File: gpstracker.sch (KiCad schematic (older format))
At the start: 52 parts, among them IC1 SIM808, J2 Leds, J3 47553-0001, J4 CONN_COAXIAL, J5 CONN_COAXIAL, J6 Micro_SD_Card, Q1 DMP1045U, SW1 Reset, U1 MCP73832-5-OT, U2 ATMEGA328P-AU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

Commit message: More routing
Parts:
- added C19: 100uF, Capacitors_SMD:CP_Elec_6.3x7.7, symbol CP
- C16: footprint Capacitors_Tantalum_SMD:CP_Tantalum_Case-T_EIA-3528-12_Hand -> Capacitors_SMD:CP_Elec_6.3x7.7; Manufacturer (none) -> Panasonic; Manufacturer part number (none) -> EEE-TPC101XAP; Package (none) -> 6.30mm
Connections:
- net +3V3: now also C19.1
- net ARD_HRX: now also U2.10 ((PCINT22/OC0A/AIN0)PD6); no longer U2.9 ((PCINT21/OC0B/T1)PD5)
- net ARD_HTX: now also U2.9 ((PCINT21/OC0B/T1)PD5); no longer U2.10 ((PCINT22/OC0A/AIN0)PD6)
- net GND: now also C19.2
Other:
- moved on the sheet: C15, C2, C5, J6, R14, R15, R4, R5, R6, SW1, U2

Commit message: Redo - Arduino, Sim & power supply
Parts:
- Q1: footprint TO_SOT_Packages_SMD:TO-252-2 -> TO_SOT_Packages_SMD:SOT-23_Handsoldering
- U1: footprint TO_SOT_Packages_SMD:SOT-23-5 -> TO_SOT_Packages_SMD:SOT-23-5_HandSoldering
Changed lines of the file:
@@
 F 0 "U1" H 1300 1550 50  0000 L CNN
 F 1 "MCP73832-5-OT" H 1650 1550 50  0000 L CNN
-F 2 "TO_SOT_Packages_SMD:SOT-23-5" H 1650 1050 50  0001 L CIN
+F 2 "TO_SOT_Packages_SMD:SOT-23-5_HandSoldering" H 1650 1050 50  0001 L CIN
 F 3 "" H 1450 1250 50  0001 C CNN
 	1    1600 1300
@@
 F 0 "Q1" V 4000 1500 50  0000 L CNN
 F 1 "DMP1045U" V 4100 1350 50  0000 L CNN
-F 2 "TO_SOT_Packages_SMD:TO-252-2" H 4000 1550 50  0001 C CNN
+F 2 "TO_SOT_Packages_SMD:SOT-23_Handsoldering" H 4000 1550 50  0001 C CNN
 F 3 "" H 3800 1450 50  0001 C CNN
 	1    3800 1450

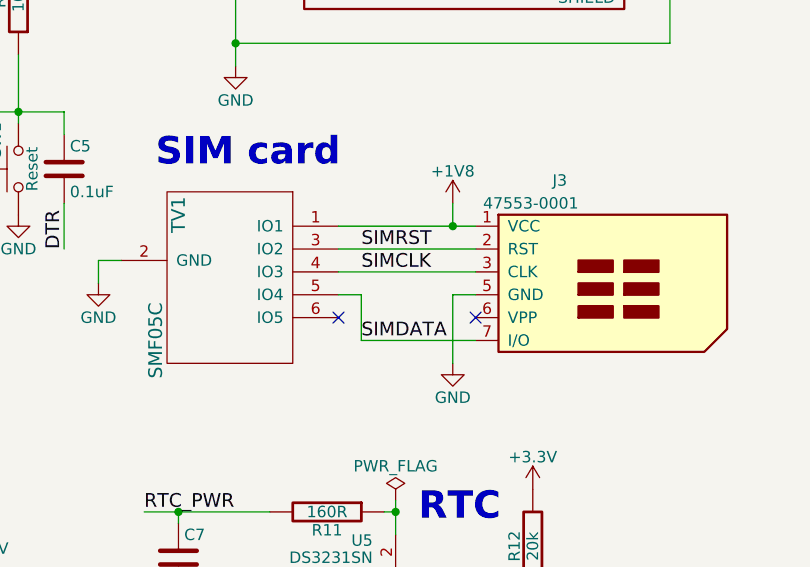
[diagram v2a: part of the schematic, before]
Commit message: Most of the routing is done (missing sdcard)
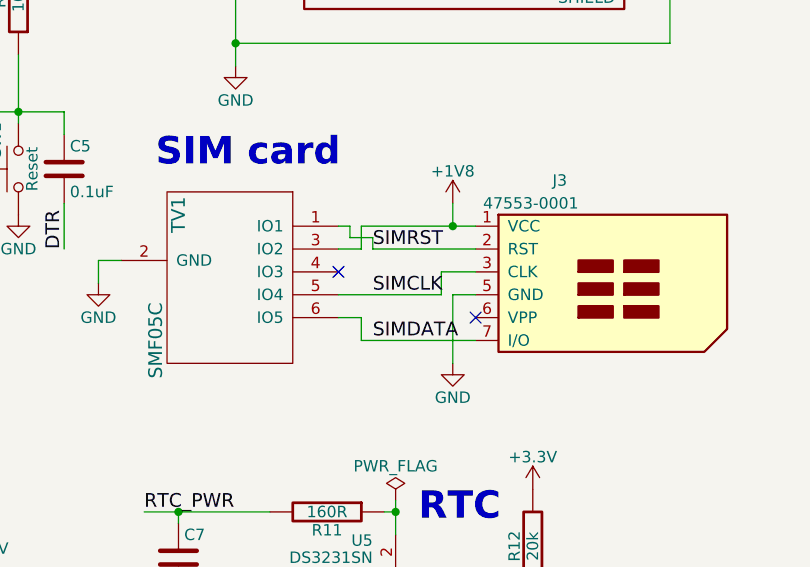
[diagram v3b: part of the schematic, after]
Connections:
- net +1V8: now also TV1.3 (IO2); no longer TV1.1 (IO1)
- net SIMCLK: now also TV1.5 (IO4); no longer TV1.4 (IO3)
- net SIMDATA: now also TV1.6 (IO5); no longer TV1.5 (IO4)
- net SIMRST: now also TV1.1 (IO1); no longer TV1.3 (IO2)

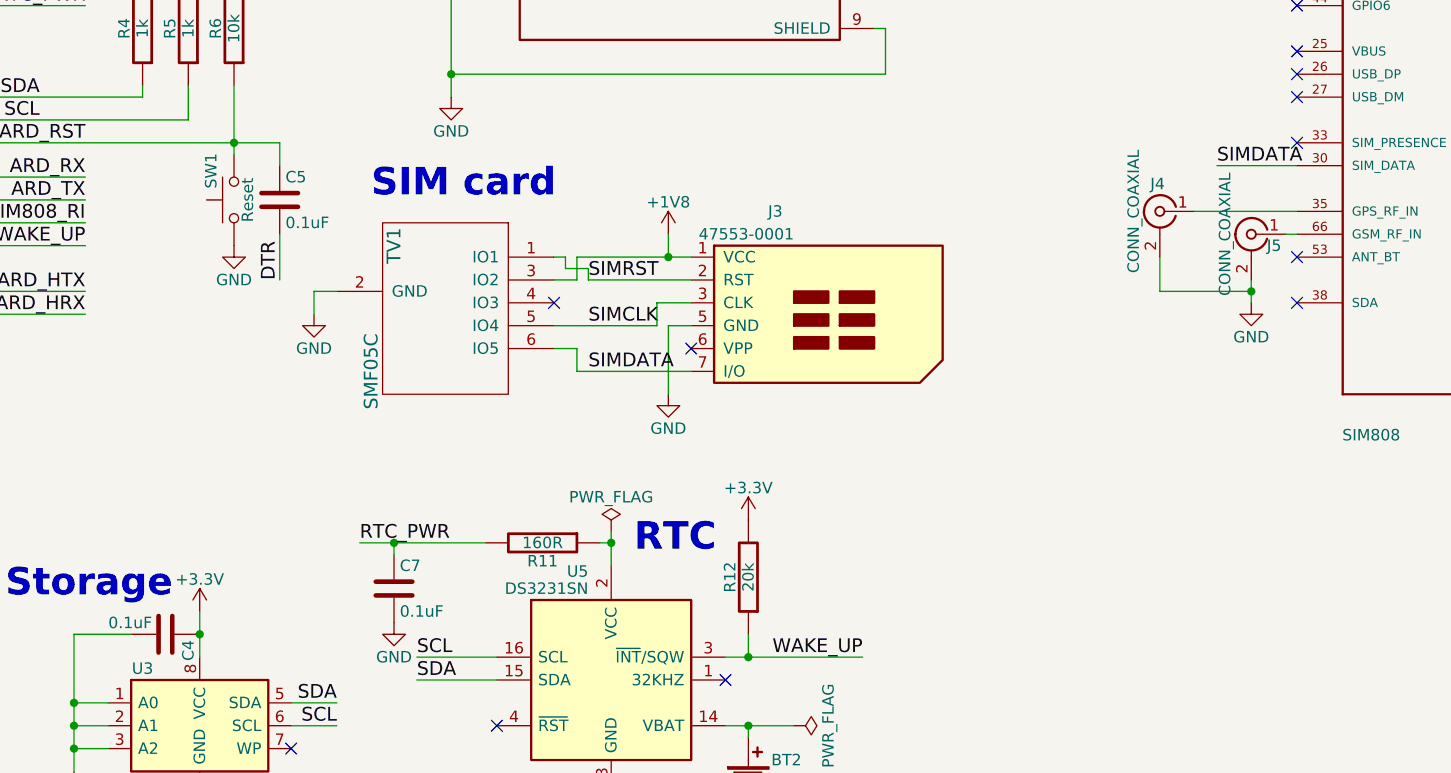
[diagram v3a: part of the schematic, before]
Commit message: Finished PCB, powering eeprom from arduino
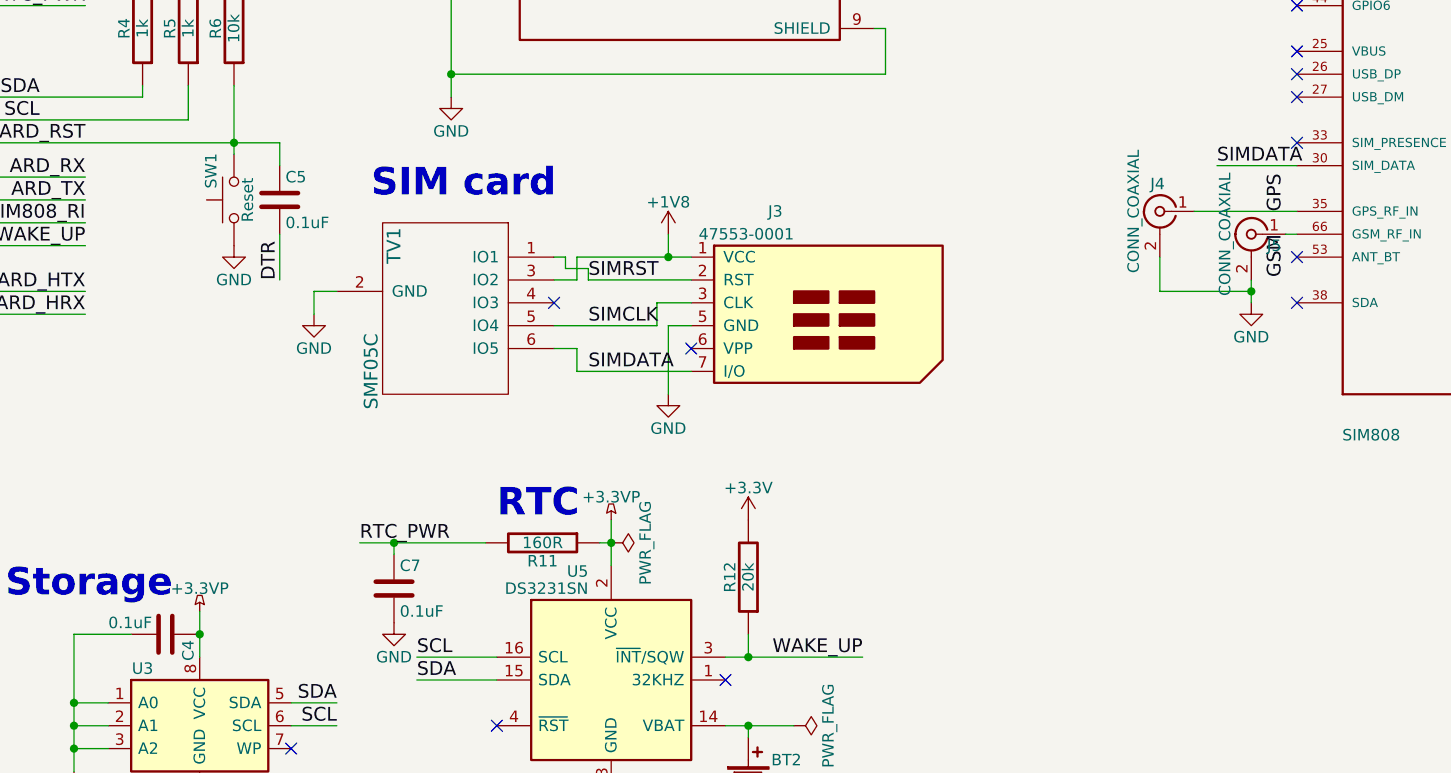
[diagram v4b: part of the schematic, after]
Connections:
- net +3V3: no longer C4.1, U3.8 (VCC)
- net +3.3VP: now reaches R11.1, U5.2 (VCC)
- net +3.3VP: now also C4.1, U3.8 (VCC)
- net GPS: now reaches IC1.35 (GPS_RF_IN), J4.1 (In)
- net GSM: now reaches IC1.66 (GSM_RF_IN), J5.1 (In)
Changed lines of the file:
@@
 LIBS:Logic_Programmable
 LIBS:Logic_TTL_IEEE
+LIBS:logo
 LIBS:maxim
 LIBS:MCU_AnalogDevices
@@
 SCL
 $Comp
-L +3.3V #PWR018
-U 1 1 5A32DA29
-P 4000 6700
-F 0 "#PWR018" H 4000 6550 50  0001 C CNN
-F 1 "+3.3V" H 4000 6840 50  0000 C CNN
-F 2 "" H 4000 6700 50  0001 C CNN
-F 3 "" H 4000 6700 50  0001 C CNN
-	1    4000 6700
-	1    0    0    -1
-$EndComp
-$Comp
-L GND #PWR019
+L GND #PWR018
 U 1 1 5A32DCCB
 P 3450 7400
-F 0 "#PWR019" H 3450 7150 50  0001 C CNN
+F 0 "#PWR018" H 3450 7150 50  0001 C CNN
 F 1 "GND" H 3450 7250 50  0000 C CNN
 F 2 "" H 3450 7400 50  0001 C CNN
@@
 SDA
 $Comp
-L +BATT #PWR020
+L +BATT #PWR019
 U 1 1 5A3327BC
 P 3450 1450
-F 0 "#PWR020" H 3450 1300 50  0001 C CNN
+F 0 "#PWR019" H 3450 1300 50  0001 C CNN
 F 1 "+BATT" H 3450 1590 50  0000 C CNN
 F 2 "" H 3450 1450 50  0001 C CNN
@@
 $EndComp
 $Comp
-L +3.3V #PWR021
+L +3.3V #PWR020
 U 1 1 5A332E51
 P 5800 950
-F 0 "#PWR021" H 5800 800 50  0001 C CNN
+F 0 "#PWR020" H 5800 800 50  0001 C CNN
 F 1 "+3.3V" H 5800 1090 50  0000 C CNN
 F 2 "" H 5800 950 50  0001 C CNN
@@
 $EndComp
 $Comp
-L GND #PWR022
+L GND #PWR021
 U 1 1 5A354AC8
 P 4300 1300
-F 0 "#PWR022" H 4300 1050 50  0001 C CNN
+F 0 "#PWR021" H 4300 1050 50  0001 C CNN
 F 1 "GND" H 4300 1150 50  0000 C CNN
 F 2 "" H 4300 1300 50  0001 C CNN
@@
 $EndComp
 $Comp
-L GND #PWR023
+L GND #PWR022
 U 1 1 5A367CD8
 P 6650 1900
-F 0 "#PWR023" H 6650 1650 50  0001 C CNN
+F 0 "#PWR022" H 6650 1650 50  0001 C CNN
 F 1 "GND" H 6650 1750 50  0000 C CNN
 F 2 "" H 6650 1900 50  0001 C CNN
@@
 	1    0    0    -1
 $EndComp
-Text Notes 5900 6450 0    120  ~ 24
+Text Notes 5300 6300 0    120  ~ 24
 RTC
 $Comp
-L GND #PWR024
+L GND #PWR023
 U 1 1 5A373D7F
 P 5800 7500
-F 0 "#PWR024" H 5800 7250 50  0001 C CNN
+F 0 "#PWR023" H 5800 7250 50  0001 C CNN
 F 1 "GND" H 5800 7350 50  0000 C CNN
 F 2 "" H 5800 7500 50  0001 C CNN
@@
 $EndComp
 $Comp
-L GND #PWR025
+L GND #PWR024
 U 1 1 5A37473D
 P 4850 6750
-F 0 "#PWR025" H 4850 6500 50  0001 C CNN
+F 0 "#PWR024" H 4850 6500 50  0001 C CNN
 F 1 "GND" H 4850 6600 50  0000 C CNN
 F 2 "" H 4850 6750 50  0001 C CNN
@@
 $EndComp
 $Comp
-L GND #PWR026
+L GND #PWR025
 U 1 1 5A37CF5A
 P 6400 7550
-F 0 "#PWR026" H 6400 7300 50  0001 C CNN
+F 0 "#PWR025" H 6400 7300 50  0001 C CNN
 F 1 "GND" H 6400 7400 50  0000 C CNN
 F 2 "" H 6400 7550 50  0001 C CNN
@@
 $EndComp
 $Comp
-L +3.3V #PWR027
+L +3.3V #PWR026
 U 1 1 5A37D38F
 P 6400 6300
-F 0 "#PWR027" H 6400 6150 50  0001 C CNN
+F 0 "#PWR026" H 6400 6150 50  0001 C CNN
 F 1 "+3.3V" H 6400 6440 50  0000 C CNN
 F 2 "" H 6400 6300 50  0001 C CNN
@@
 $EndComp
 $Comp
-L GND #PWR028
+L GND #PWR027
 U 1 1 5A3871D1
 P 2750 1950
-F 0 "#PWR028" H 2750 1700 50  0001 C CNN
+F 0 "#PWR027" H 2750 1700 50  0001 C CNN
 F 1 "GND" H 2750 1800 50  0000 C CNN
 F 2 "" H 2750 1950 50  0001 C CNN
@@
 NoConn ~ 1150 4650
 $Comp
-L PWR_FLAG #FLG029
+L PWR_FLAG #FLG028
 U 1 1 5A38FA4F
 P 6600 7200
-F 0 "#FLG029" H 6600 7275 50  0001 C CNN
+F 0 "#FLG028" H 6600 7275 50  0001 C CNN
 F 1 "PWR_FLAG" H 6600 7350 50  0000 C CNN
 F 2 "" H 6600 7200 50  0001 C CNN
@@
 $EndComp
 $Comp
+L PWR_FLAG #FLG029
+U 1 1 5A3900F9
+P 5800 6400
+F 0 "#FLG029" H 5800 6475 50  0001 C CNN
+F 1 "PWR_FLAG" H 5800 6550 50  0000 C CNN
+F 2 "" H 5800 6400 50  0001 C CNN
+F 3 "" H 5800 6400 50  0001 C CNN
+	1    5800 6400
+	0    1    1    0
+$EndComp
+$Comp
 L PWR_FLAG #FLG030
-U 1 1 5A3900F9
-P 5800 6350
-F 0 "#FLG030" H 5800 6425 50  0001 C CNN
-F 1 "PWR_FLAG" H 5800 6500 50  0000 C CNN
-F 2 "" H 5800 6350 50  0001 C CNN
-F 3 "" H 5800 6350 50  0001 C CNN
-	1    5800 6350
-	1    0    0    -1
-$EndComp
-$Comp
-L PWR_FLAG #FLG031
 U 1 1 5A39252B
 P 4350 1550
-F 0 "#FLG031" H 4350 1625 50  0001 C CNN
+F 0 "#FLG030" H 4350 1625 50  0001 C CNN
 F 1 "PWR_FLAG" H 4350 1700 50  0000 C CNN
 F 2 "" H 4350 1550 50  0001 C CNN
@@
 $EndComp
 $Comp
-L +3.3V #PWR032
+L +3.3V #PWR031
 U 1 1 5A393FBC
 P 7250 900
-F 0 "#PWR032" H 7250 750 50  0001 C CNN
+F 0 "#PWR031" H 7250 750 50  0001 C CNN
 F 1 "+3.3V" H 7250 1040 50  0000 C CNN
 F 2 "" H 7250 900 50  0001 C CNN
@@
 $EndComp
 $Comp
-L GND #PWR033
+L GND #PWR032
 U 1 1 5A39AF3D
 P 10450 5700
-F 0 "#PWR033" H 10450 5450 50  0001 C CNN
+F 0 "#PWR032" H 10450 5450 50  0001 C CNN
 F 1 "GND" H 10450 5550 50  0000 C CNN
 F 2 "" H 10450 5700 50  0001 C CNN
@@
 SIMDATA
 $Comp
-L +1V8 #PWR034
+L +1V8 #PWR033
 U 1 1 5A39C52E
 P 10450 4600
-F 0 "#PWR034" H 10450 4450 50  0001 C CNN
+F 0 "#PWR033" H 10450 4450 50  0001 C CNN
 F 1 "+1V8" H 10450 4740 50  0000 C CNN
 F 2 "" H 10450 4600 50  0001 C CNN
@@
 NoConn ~ 8800 4650
 $Comp
-L +2V8 #PWR035
+L +2V8 #PWR034
 U 1 1 5A3A032F
 P 10450 1500
-F 0 "#PWR035" H 10450 1350 50  0001 C CNN
+F 0 "#PWR034" H 10450 1350 50  0001 C CNN
 F 1 "+2V8" H 10450 1640 50  0000 C CNN
 F 2 "" H 10450 1500 50  0001 C CNN
@@
 $EndComp
 $Comp
-L GND #PWR036
+L GND #PWR035
 U 1 1 5A3A071B
 P 10700 1600
-F 0 "#PWR036" H 10700 1350 50  0001 C CNN
+F 0 "#PWR035" H 10700 1350 50  0001 C CNN
 F 1 "GND" H 10700 1450 50  0000 C CNN
 F 2 "" H 10700 1600 50  0001 C CNN
@@
 $EndComp
 $Comp
-L +BATT #PWR037
+L +BATT #PWR036
 U 1 1 5A3A0C70
 P 10450 1100
-F 0 "#PWR037" H 10450 950 50  0001 C CNN
+F 0 "#PWR036" H 10450 950 50  0001 C CNN
 F 1 "+BATT" H 10450 1240 50  0000 C CNN
 F 2 "" H 10450 1100 50  0001 C CNN
@@
 NoConn ~ 8800 5150
 $Comp
-L GND #PWR038
+L GND #PWR037
 U 1 1 5A3A2FD9
 P 8600 5350
-F 0 "#PWR038" H 8600 5100 50  0001 C CNN
+F 0 "#PWR037" H 8600 5100 50  0001 C CNN
 F 1 "GND" H 8600 5200 50  0000 C CNN
 F 2 "" H 8600 5350 50  0001 C CNN
@@
 $EndComp
 $Comp
-L +2V8 #PWR039
+L +2V8 #PWR038
 U 1 1 5A3A5C32
 P 8650 2400
-F 0 "#PWR039" H 8650 2250 50  0001 C CNN
+F 0 "#PWR038" H 8650 2250 50  0001 C CNN
 F 1 "+2V8" H 8650 2540 50  0000 C CNN
 F 2 "" H 8650 2400 50  0001 C CNN
@@
 $EndComp
 $Comp
-L +3.3V #PWR040
+L +3.3V #PWR039
 U 1 1 5A3AF4E3
 P 3950 3800
-F 0 "#PWR040" H 3950 3650 50  0001 C CNN
+F 0 "#PWR039" H 3950 3650 50  0001 C CNN
 F 1 "+3.3V" H 3950 3940 50  0000 C CNN
 F 2 "" H 3950 3800 50  0001 C CNN
@@
 $EndSheet
 $Comp
-L VBUS #PWR041
+L VBUS #PWR040
 U 1 1 5A36D4DE
 P 1600 750
-F 0 "#PWR041" H 1600 600 50  0001 C CNN
+F 0 "#PWR040" H 1600 600 50  0001 C CNN
 F 1 "VBUS" H 1600 900 50  0000 C CNN
 F 2 "" H 1600 750 50  0001 C CNN
@@
 $EndComp
 $Comp
-L VBUS #PWR042
+L VBUS #PWR041
 U 1 1 5A36D854
 P 3800 750
-F 0 "#PWR042" H 3800 600 50  0001 C CNN
+F 0 "#PWR041" H 3800 600 50  0001 C CNN
 F 1 "VBUS" H 3800 900 50  0000 C CNN
 F 2 "" H 3800 750 50  0001 C CNN
@@
 ARD_RX
 $Comp
-L GND #PWR043
+L GND #PWR042
 U 1 1 5A37400C
 P 1250 7200
-F 0 "#PWR043" H 1250 6950 50  0001 C CNN
+F 0 "#PWR042" H 1250 6950 50  0001 C CNN
 F 1 "GND" H 1250 7050 50  0000 C CNN
 F 2 "" H 1250 7200 50  0001 C CNN
@@
 $EndComp
 $Comp
-L GND #PWR044
+L GND #PWR043
 U 1 1 5A378081
 P 800 3650
-F 0 "#PWR044" H 800 3400 50  0001 C CNN
+F 0 "#PWR043" H 800 3400 50  0001 C CNN
 F 1 "GND" H 800 3500 50  0000 C CNN
 F 2 "" H 800 3650 50  0001 C CNN
@@
 $EndComp
 $Comp
-L +BATT #PWR045
+L +BATT #PWR044
 U 1 1 5A37F063
 P 7450 2100
-F 0 "#PWR045" H 7450 1950 50  0001 C CNN
+F 0 "#PWR044" H 7450 1950 50  0001 C CNN
 F 1 "+BATT" H 7450 2240 50  0000 C CNN
 F 2 "" H 7450 2100 50  0001 C CNN
@@
 $EndComp
 $Comp
-L GND #PWR046
+L GND #PWR045
 U 1 1 5A37F86E
 P 7450 2600
-F 0 "#PWR046" H 7450 2350 50  0001 C CNN
+F 0 "#PWR045" H 7450 2350 50  0001 C CNN
 F 1 "GND" H 7450 2450 50  0000 C CNN
 F 2 "" H 7450 2600 50  0001 C CNN
@@
 $EndComp
 $Comp
-L GND #PWR047
+L GND #PWR046
 U 1 1 5A38E1D4
 P 600 3650
-F 0 "#PWR047" H 600 3400 50  0001 C CNN
+F 0 "#PWR046" H 600 3400 50  0001 C CNN
 F 1 "GND" H 600 3500 50  0000 C CNN
 F 2 "" H 600 3650 50  0001 C CNN
@@
 	4700 6400 5250 6400
 Wire Wire Line
-	5800 6350 5800 6500
+	5800 6300 5800 6500
 Connection ~ 6400 6900
 Wire Wire Line
@@
 	6000 5350 6150 5350
 NoConn ~ 5550 5350
+$Comp
+L +3.3VP #PWR047
+U 1 1 5A41A5CD
+P 5800 6300
+F 0 "#PWR047" H 5950 6250 50  0001 C CNN
+F 1 "+3.3VP" H 5800 6400 50  0000 C CNN
+F 2 "" H 5800 6300 50  0001 C CNN
+F 3 "" H 5800 6300 50  0001 C CNN
+	1    5800 6300
+	1    0    0    -1
+$EndComp
+$Comp
+L +3.3VP #PWR048
+U 1 1 5A41B236
+P 4000 6700
+F 0 "#PWR048" H 4150 6650 50  0001 C CNN
+F 1 "+3.3VP" H 4000 6800 50  0000 C CNN
+F 2 "" H 4000 6700 50  0001 C CNN
+F 3 "" H 4000 6700 50  0001 C CNN
+	1    4000 6700
+	1    0    0    -1
+$EndComp
+Text Label 8750 4950 1    60   ~ 0
+GPS
+Text Label 8750 5050 3    60   ~ 0
+GSM
 $EndSCHEMATC
